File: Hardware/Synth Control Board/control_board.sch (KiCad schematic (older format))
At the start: 44 parts, among them J1 Conn_01x13, J2 Conn_01x03, J3 Conn_01x13, J4 Conn_01x13, J5 Conn_01x02, J6 Conn_01x13, SW1 SW_DPDT_x2, SW10 SW_SPST, SW11 SW_SPST, SW12 SW_SPST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

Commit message: add frequency and LFO connectors to control board
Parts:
- added J10, J7, J8, J9: Conn_01x05, Pin_Headers:Pin_Header_Straight_1x05_Pitch2.54mm, symbol Conn_01x05
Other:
- moved on the sheet: J2, J5, RV5, SW1A
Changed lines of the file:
@@
 L POT RV5
 U 1 1 5C5C948E
-P 1500 6350
-F 0 "RV5" V 1325 6350 50  0000 C CNN
-F 1 "10kA" V 1400 6350 50  0000 C CNN
-F 2 "Potentiometers:Potentiometer_Bourns_PTV09A-1_Horizontal" H 1500 6350 50  0001 C CNN
-F 3 "" H 1500 6350 50  0001 C CNN
-	1    1500 6350
+P 1500 5800
+F 0 "RV5" V 1325 5800 50  0000 C CNN
+F 1 "10kA" V 1400 5800 50  0000 C CNN
+F 2 "Potentiometers:Potentiometer_Bourns_PTV09A-1_Horizontal" H 1500 5800 50  0001 C CNN
+F 3 "" H 1500 5800 50  0001 C CNN
+	1    1500 5800
 	0    1    1    0
 $EndComp
@@
 Text Label 3000 7150 2    60   ~ 0
 freq_in_4
-Text Label 13000 2600 2    60   ~ 0
+Text Label 10400 3850 2    60   ~ 0
 freq_in_1
 Text Label 4250 5650 0    60   ~ 0
@@
 Text Label 4250 7150 0    60   ~ 0
 freq_out_4
-Text Label 13000 2800 2    60   ~ 0
+Text Label 10400 4050 2    60   ~ 0
 freq_out_1
-Text Label 1150 6350 2    60   ~ 0
+Text Label 1150 5800 2    60   ~ 0
 LFO_freq_in
-Text Label 1750 6350 0    60   ~ 0
+Text Label 1750 5800 0    60   ~ 0
 LFO_freq_out
-Text Label 10450 5200 2    60   ~ 0
+Text Label 1550 6400 2    60   ~ 0
 LFO_freq_in
-Text Label 10450 5300 2    60   ~ 0
+Text Label 1550 6500 2    60   ~ 0
 LFO_freq_out
 $Comp
@@
 L Conn_01x02 J5
 U 1 1 5C5CD696
-P 10800 5200
-F 0 "J5" H 10800 5300 50  0000 C CNN
-F 1 "Conn_01x02" H 10800 5000 50  0000 C CNN
-F 2 "Pin_Headers:Pin_Header_Straight_1x02_Pitch2.54mm" H 10800 5200 50  0001 C CNN
-F 3 "" H 10800 5200 50  0001 C CNN
-	1    10800 5200
-	1    0    0    -1
-$EndComp
-Wire Wire Line
-	10600 5200 10450 5200
-Wire Wire Line
-	10450 5300 10600 5300
+P 1900 6400
+F 0 "J5" H 1900 6500 50  0000 C CNN
+F 1 "Conn_01x02" H 1900 6200 50  0000 C CNN
+F 2 "Pin_Headers:Pin_Header_Straight_1x02_Pitch2.54mm" H 1900 6400 50  0001 C CNN
+F 3 "" H 1900 6400 50  0001 C CNN
+	1    1900 6400
+	1    0    0    -1
+$EndComp
+Wire Wire Line
+	1700 6400 1550 6400
+Wire Wire Line
+	1550 6500 1700 6500
 Wire Wire Line
 	3350 5450 3350 5400
@@
 Connection ~ 3650 7150
 Wire Wire Line
-	1500 6500 1500 6550
-Wire Wire Line
-	1500 6550 1300 6550
-Wire Wire Line
-	1300 6550 1300 6350
-Wire Wire Line
-	1150 6350 1350 6350
-Connection ~ 1300 6350
-Wire Wire Line
-	1750 6350 1650 6350
+	1500 5950 1500 6000
+Wire Wire Line
+	1500 6000 1300 6000
+Wire Wire Line
+	1300 6000 1300 5800
+Wire Wire Line
+	1150 5800 1350 5800
+Connection ~ 1300 5800
+Wire Wire Line
+	1750 5800 1650 5800
 $Comp
 L +5V #PWR024
@@
 	3550 6850 3550 7150
 Connection ~ 3550 7150
-Text Label 13000 2700 2    60   ~ 0
+Text Label 10400 3950 2    60   ~ 0
 freq_fb_1
 $Comp
 L SW_DPDT_x2 SW1
 U 1 1 5C5E11B0
-P 10050 5950
-F 0 "SW1" H 10050 6120 50  0000 C CNN
-F 1 "SW_DPDT_x2" H 10300 5950 50  0000 C CNN
-F 2 "SparkFun-Electromechanical:SWITCH-SPDT" H 10050 5950 50  0001 C CNN
-F 3 "" H 10050 5950 50  0001 C CNN
-	1    10050 5950
+P 1150 7150
+F 0 "SW1" H 1150 7320 50  0000 C CNN
+F 1 "SW_DPDT_x2" H 1400 7150 50  0000 C CNN
+F 2 "SparkFun-Electromechanical:SWITCH-SPDT" H 1150 7150 50  0001 C CNN
+F 3 "" H 1150 7150 50  0001 C CNN
+	1    1150 7150
 	-1   0    0    -1
 $EndComp
@@
 L Conn_01x03 J2
 U 1 1 5C5E130C
-P 10900 5950
-F 0 "J2" H 10900 6150 50  0000 C CNN
-F 1 "Conn_01x03" H 10900 5750 50  0000 C CNN
-F 2 "Pin_Headers:Pin_Header_Straight_1x03_Pitch2.54mm" H 10900 5950 50  0001 C CNN
-F 3 "" H 10900 5950 50  0001 C CNN
-	1    10900 5950
-	1    0    0    -1
-$EndComp
-Wire Wire Line
-	10700 5950 10250 5950
-Wire Wire Line
-	10700 5850 10400 5850
-Wire Wire Line
-	10400 5850 10400 5700
-Wire Wire Line
-	10400 5700 9750 5700
-Wire Wire Line
-	9750 5700 9750 5850
-Wire Wire Line
-	9750 5850 9850 5850
-Wire Wire Line
-	9850 6050 9750 6050
-Wire Wire Line
-	9750 6050 9750 6250
-Wire Wire Line
-	9750 6250 10400 6250
-Wire Wire Line
-	10400 6250 10400 6050
-Wire Wire Line
-	10400 6050 10700 6050
-Text Label 9850 5700 0    60   ~ 0
+P 2000 7150
+F 0 "J2" H 2000 7350 50  0000 C CNN
+F 1 "Conn_01x03" H 2000 6950 50  0000 C CNN
+F 2 "Pin_Headers:Pin_Header_Straight_1x03_Pitch2.54mm" H 2000 7150 50  0001 C CNN
+F 3 "" H 2000 7150 50  0001 C CNN
+	1    2000 7150
+	1    0    0    -1
+$EndComp
+Wire Wire Line
+	1800 7150 1350 7150
+Wire Wire Line
+	1800 7050 1500 7050
+Wire Wire Line
+	1500 7050 1500 6900
+Wire Wire Line
+	1500 6900 850  6900
+Wire Wire Line
+	850  6900 850  7050
+Wire Wire Line
+	850  7050 950  7050
+Wire Wire Line
+	950  7250 850  7250
+Wire Wire Line
+	850  7250 850  7450
+Wire Wire Line
+	850  7450 1500 7450
+Wire Wire Line
+	1500 7450 1500 7250
+Wire Wire Line
+	1500 7250 1800 7250
+Text Label 950  6900 0    60   ~ 0
 LFO_square
-Text Label 9950 6250 0    60   ~ 0
+Text Label 1050 7450 0    60   ~ 0
 LFO_tri
-Text Label 10300 5950 0    60   ~ 0
+Text Label 1400 7150 0    60   ~ 0
 LFO_out
 $Comp
@@
 Wire Wire Line
 	6700 5750 6950 5750
-Text Label 13000 2900 2    60   ~ 0
+Text Label 10400 4150 2    60   ~ 0
 lfo_in_1
-Text Label 13000 3000 2    60   ~ 0
+Text Label 10400 4250 2    60   ~ 0
 lfo_out_1
 $Comp
@@
 Text Label 7250 2750 2    60   ~ 0
 osc2_quant
-Text Label 12600 3600 0    60   ~ 0
+Text Label 10400 4500 2    60   ~ 0
 freq_in_2
-Text Label 12600 3400 0    60   ~ 0
+Text Label 10400 4700 2    60   ~ 0
 freq_out_2
 $Comp
@@
 	0    1    -1   0
 $EndComp
-Text Label 12600 3500 0    60   ~ 0
+Text Label 10400 4600 2    60   ~ 0
 freq_fb_2
-Text Label 12600 3700 0    60   ~ 0
+Text Label 10400 4800 2    60   ~ 0
 lfo_in_2
-Text Label 12600 3800 0    60   ~ 0
+Text Label 10400 4900 2    60   ~ 0
 lfo_out_2
 $Comp
@@
 Text Label 8800 2400 2    60   ~ 0
 osc3_quant
-Text Label 14100 3150 2    60   ~ 0
+Text Label 10400 5200 2    60   ~ 0
 freq_in_3
-Text Label 14100 2950 2    60   ~ 0
+Text Label 10400 5400 2    60   ~ 0
 freq_out_3
 $Comp
@@
 	0    1    -1   0
 $EndComp
-Text Label 14100 3050 2    60   ~ 0
+Text Label 10400 5300 2    60   ~ 0
 freq_fb_3
-Text Label 14100 3350 2    60   ~ 0
+Text Label 10400 5500 2    60   ~ 0
 lfo_in_3
-Text Label 14100 3250 2    60   ~ 0
+Text Label 10400 5600 2    60   ~ 0
 lfo_out_3
 $Comp
@@
 Text Label 10400 2400 2    60   ~ 0
 osc4_quant
-Text Label 14600 3150 0    60   ~ 0
+Text Label 10400 5900 2    60   ~ 0
 freq_in_4
-Text Label 14600 2950 0    60   ~ 0
+Text Label 10400 6100 2    60   ~ 0
 freq_out_4
 $Comp
@@
 	0    1    -1   0
 $EndComp
-Text Label 14600 3050 0    60   ~ 0
+Text Label 10400 6000 2    60   ~ 0
 freq_fb_4
-Text Label 14600 3250 0    60   ~ 0
+Text Label 10400 6200 2    60   ~ 0
 lfo_in_4
-Text Label 14600 3350 0    60   ~ 0
+Text Label 10400 6300 2    60   ~ 0
 lfo_out_4
 $Comp
@@
 	1    0    0    -1
 $EndComp
+$Comp
+L Conn_01x05 J7
+U 1 1 5C63B7E7
+P 10600 4050
+F 0 "J7" H 10600 4350 50  0000 C CNN
+F 1 "Conn_01x05" H 10600 3750 50  0000 C CNN
+F 2 "Pin_Headers:Pin_Header_Straight_1x05_Pitch2.54mm" H 10600 4050 50  0001 C CNN
+F 3 "" H 10600 4050 50  0001 C CNN
+	1    10600 4050
+	1    0    0    -1
+$EndComp
+$Comp
+L Conn_01x05 J8
+U 1 1 5C63B889
+P 10600 4700
+F 0 "J8" H 10600 5000 50  0000 C CNN
+F 1 "Conn_01x05" H 10600 4400 50  0000 C CNN
+F 2 "Pin_Headers:Pin_Header_Straight_1x05_Pitch2.54mm" H 10600 4700 50  0001 C CNN
+F 3 "" H 10600 4700 50  0001 C CNN
+	1    10600 4700
+	1    0    0    -1
+$EndComp
+$Comp
+L Conn_01x05 J9
+U 1 1 5C63BBB5
+P 10600 5400
+F 0 "J9" H 10600 5700 50  0000 C CNN
+F 1 "Conn_01x05" H 10600 5100 50  0000 C CNN
+F 2 "Pin_Headers:Pin_Header_Straight_1x05_Pitch2.54mm" H 10600 5400 50  0001 C CNN
+F 3 "" H 10600 5400 50  0001 C CNN
+	1    10600 5400
+	1    0    0    -1
+$EndComp
+$Comp
+L Conn_01x05 J10
+U 1 1 5C63BC62
+P 10600 6100
+F 0 "J10" H 10600 6400 50  0000 C CNN
+F 1 "Conn_01x05" H 10600 5800 50  0000 C CNN
+F 2 "Pin_Headers:Pin_Header_Straight_1x05_Pitch2.54mm" H 10600 6100 50  0001 C CNN
+F 3 "" H 10600 6100 50  0001 C CNN
+	1    10600 6100
+	1    0    0    -1
+$EndComp

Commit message: match relative connector placement between two boards
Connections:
- net labels removed: GNDD

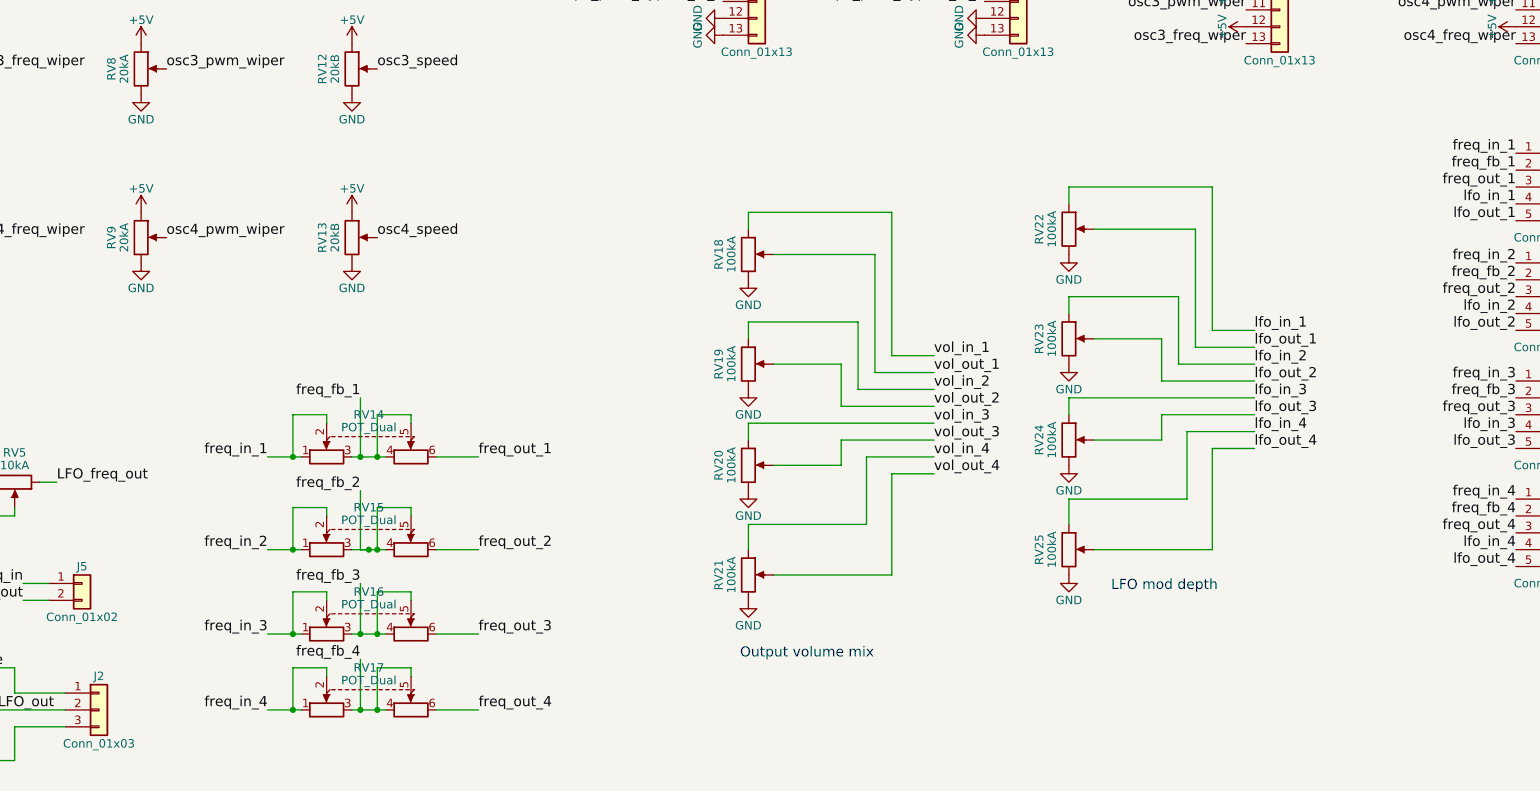
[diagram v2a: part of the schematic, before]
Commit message: add delay connector to main board and route it.
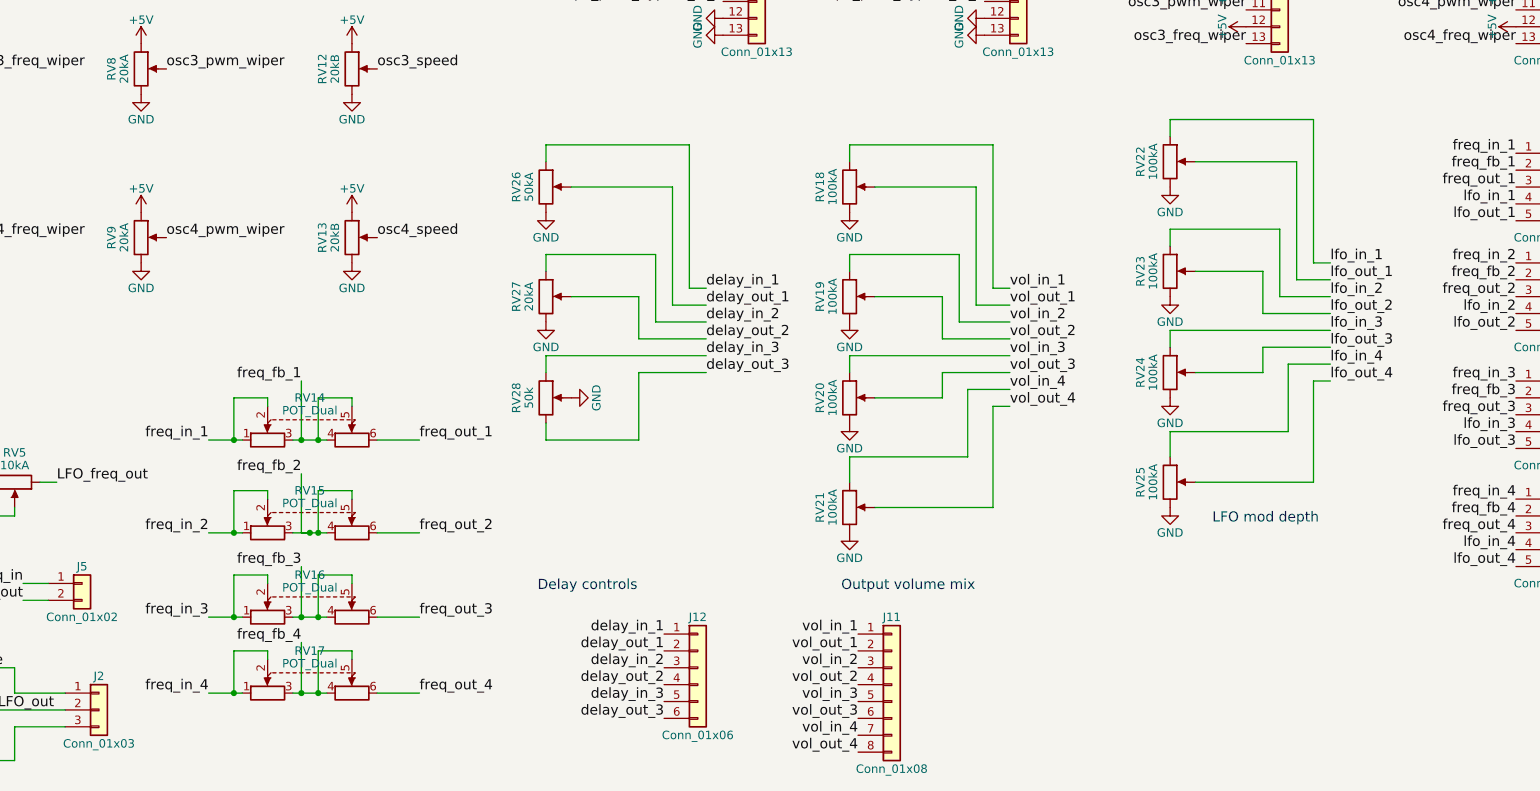
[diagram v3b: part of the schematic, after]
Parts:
- added J11: Conn_01x08, Pin_Headers:Pin_Header_Straight_1x08_Pitch2.54mm, symbol Conn_01x08
- added J12: Conn_01x06, Pin_Headers:Pin_Header_Straight_1x06_Pitch2.54mm, symbol Conn_01x06
- added RV26: 50kA, Potentiometers:Potentiometer_Bourns_PTV09A-1_Horizontal, symbol POT
- added RV27: 20kA, Potentiometers:Potentiometer_Bourns_PTV09A-1_Horizontal, symbol POT
- added RV28: 50k, Potentiometers:Potentiometer_Bourns_PTV09A-1_Horizontal, symbol POT
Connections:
- net GND: now also RV26.3, RV27.3, RV28.2
- net vol_in_1: now also J11.1 (Pin_1)
- net vol_in_2: now also J11.3 (Pin_3)
- net vol_in_3: now also J11.5 (Pin_5)
- net vol_in_4: now also J11.7 (Pin_7)
- net vol_out_1: now also J11.2 (Pin_2)
- net vol_out_2: now also J11.4 (Pin_4)
- net vol_out_3: now also J11.6 (Pin_6)
- net vol_out_4: now also J11.8 (Pin_8)
- new net delay_in_1: J12.1 (Pin_1), RV26.1
- new net delay_in_2: J12.3 (Pin_3), RV27.1
- new net delay_in_3: J12.5 (Pin_5), RV28.1
- new net delay_out_1: J12.2 (Pin_2), RV26.2
- new net delay_out_2: J12.4 (Pin_4), RV27.2
- new net delay_out_3: J12.6 (Pin_6), RV28.3
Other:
- note added: "Delay controls"
- moved on the sheet: RV14, RV15, RV16, RV17, RV18, RV19, RV20, RV21, RV22, RV23, RV24, RV25

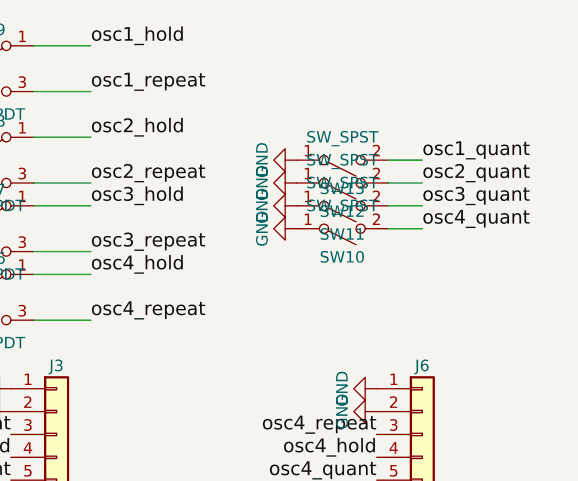
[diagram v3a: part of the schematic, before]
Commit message: fix delay controls on panel artwork and control board layout
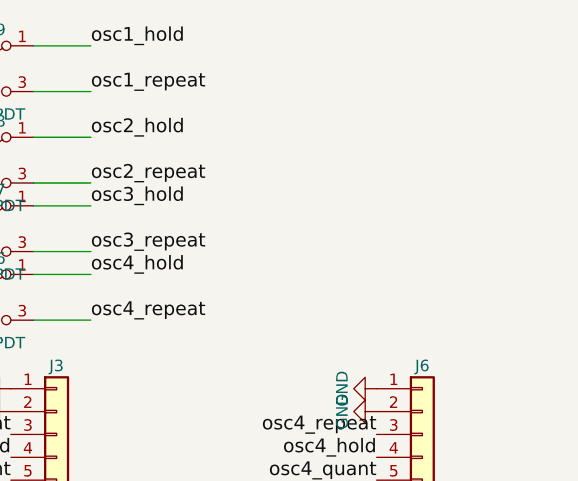
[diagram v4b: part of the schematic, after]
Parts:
- removed SW10, SW11, SW12, SW13: SW_SPST, SparkFun-Electromechanical:SWITCH-SPDT, symbol SW_SPST
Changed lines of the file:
@@
 Text Label 9150 1700 0    60   ~ 0
 osc4_repeat
-$Comp
-L SW_SPST SW13
-U 1 1 5C54E122
-P 10250 1000
-F 0 "SW13" H 10250 1125 50  0000 C CNN
-F 1 "SW_SPST" H 10250 900 50  0000 C CNN
-F 2 "SparkFun-Electromechanical:SWITCH-SPDT" H 10250 1000 50  0001 C CNN
-F 3 "" H 10250 1000 50  0001 C CNN
-	1    10250 1000
-	1    0    0    1
-$EndComp
-$Comp
-L SW_SPST SW12
-U 1 1 5C54E07F
-P 10250 1100
-F 0 "SW12" H 10250 1225 50  0000 C CNN
-F 1 "SW_SPST" H 10250 1000 50  0000 C CNN
-F 2 "SparkFun-Electromechanical:SWITCH-SPDT" H 10250 1100 50  0001 C CNN
-F 3 "" H 10250 1100 50  0001 C CNN
-	1    10250 1100
-	1    0    0    1
-$EndComp
-$Comp
-L SW_SPST SW11
-U 1 1 5C54DFDF
-P 10250 1200
-F 0 "SW11" H 10250 1325 50  0000 C CNN
-F 1 "SW_SPST" H 10250 1100 50  0000 C CNN
-F 2 "SparkFun-Electromechanical:SWITCH-SPDT" H 10250 1200 50  0001 C CNN
-F 3 "" H 10250 1200 50  0001 C CNN
-	1    10250 1200
-	1    0    0    1
-$EndComp
-$Comp
-L SW_SPST SW10
-U 1 1 5C54DEFF
-P 10250 1300
-F 0 "SW10" H 10250 1425 50  0000 C CNN
-F 1 "SW_SPST" H 10250 1200 50  0000 C CNN
-F 2 "SparkFun-Electromechanical:SWITCH-SPDT" H 10250 1300 50  0001 C CNN
-F 3 "" H 10250 1300 50  0001 C CNN
-	1    10250 1300
-	1    0    0    1
-$EndComp
-Text Label 10600 1000 0    60   ~ 0
-osc1_quant
-Text Label 10600 1100 0    60   ~ 0
-osc2_quant
-Text Label 10600 1200 0    60   ~ 0
-osc3_quant
-Text Label 10600 1300 0    60   ~ 0
-osc4_quant
 Text Label 6000 1300 2    60   ~ 0
 envelope_pwm_bypass_in_4
@@
 Text Label 5700 2750 2    60   ~ 0
 osc1_quant
-Wire Wire Line
-	10600 1300 10450 1300
-Wire Wire Line
-	10450 1200 10600 1200
-Wire Wire Line
-	10600 1100 10450 1100
-Wire Wire Line
-	10450 1000 10600 1000
 Text Label 2650 5550 2    60   ~ 0
 freq_in_1
@@
 	0    1    1    0
 $EndComp
-$Comp
-L GND #PWR057
-U 1 1 5C638574
-P 10050 1000
-F 0 "#PWR057" H 10050 750 50  0001 C CNN
-F 1 "GND" H 10050 850 50  0000 C CNN
-F 2 "" H 10050 1000 50  0001 C CNN
-F 3 "" H 10050 1000 50  0001 C CNN
-	1    10050 1000
-	0    1    1    0
-$EndComp
-$Comp
-L GND #PWR058
-U 1 1 5C63860F
-P 10050 1100
-F 0 "#PWR058" H 10050 850 50  0001 C CNN
-F 1 "GND" H 10050 950 50  0000 C CNN
-F 2 "" H 10050 1100 50  0001 C CNN
-F 3 "" H 10050 1100 50  0001 C CNN
-	1    10050 1100
-	0    1    1    0
-$EndComp
-$Comp
-L GND #PWR059
-U 1 1 5C6386AA
-P 10050 1200
-F 0 "#PWR059" H 10050 950 50  0001 C CNN
-F 1 "GND" H 10050 1050 50  0000 C CNN
-F 2 "" H 10050 1200 50  0001 C CNN
-F 3 "" H 10050 1200 50  0001 C CNN
-	1    10050 1200
-	0    1    1    0
-$EndComp
-$Comp
-L GND #PWR060
-U 1 1 5C638745
-P 10050 1300
-F 0 "#PWR060" H 10050 1050 50  0001 C CNN
-F 1 "GND" H 10050 1150 50  0000 C CNN
-F 2 "" H 10050 1300 50  0001 C CNN
-F 3 "" H 10050 1300 50  0001 C CNN
-	1    10050 1300
-	0    1    1    0
-$EndComp

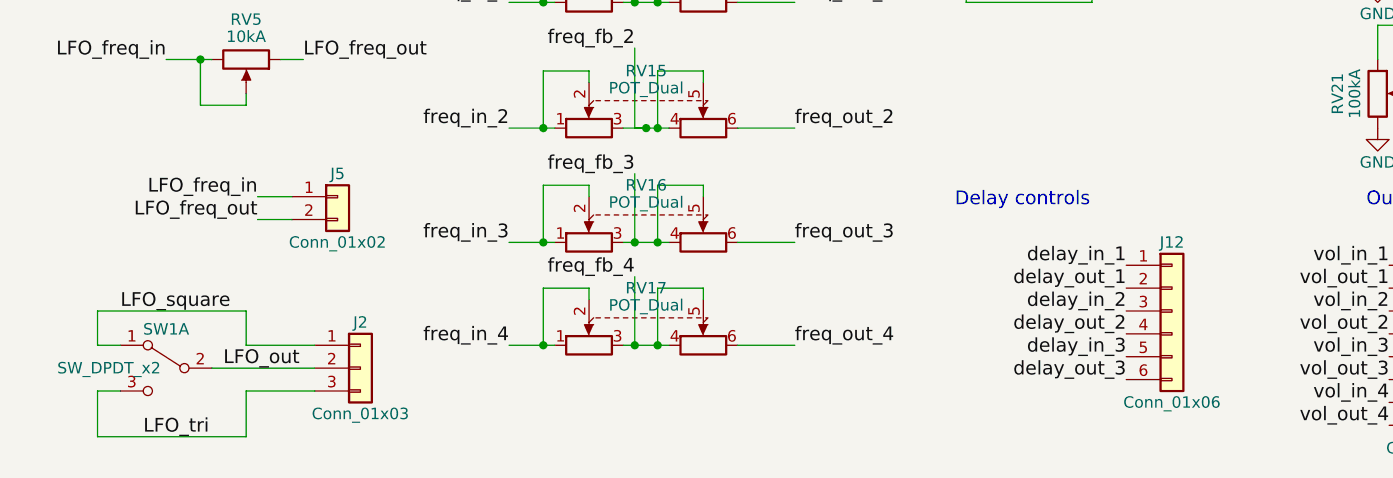
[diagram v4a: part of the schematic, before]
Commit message: move main synth board so that connector dimensions match between boards.
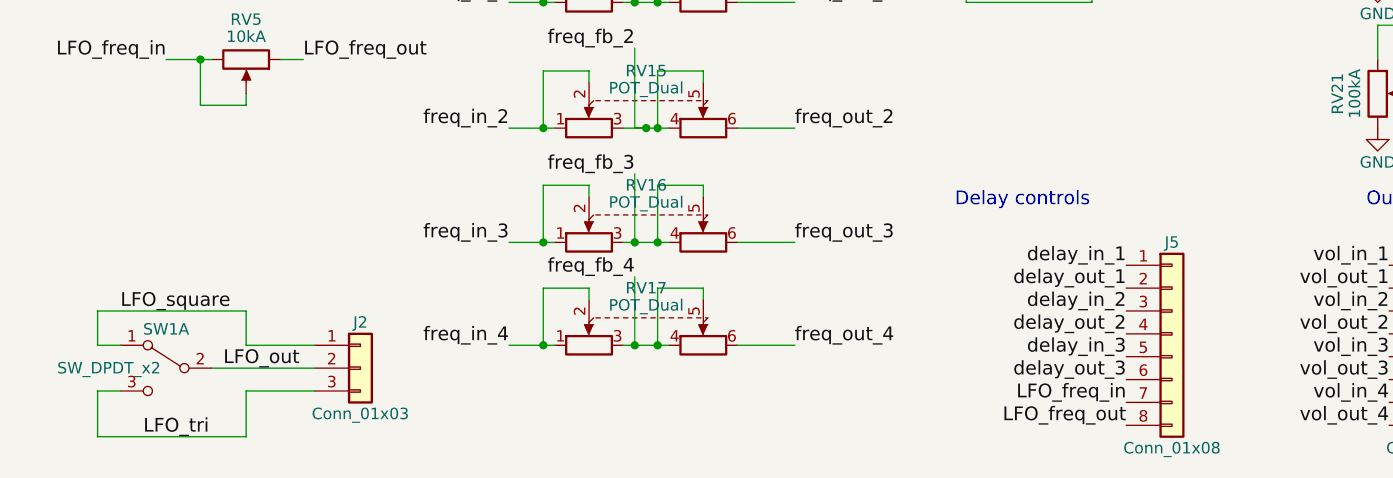
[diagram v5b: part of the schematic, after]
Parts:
- removed J12: Conn_01x06, Pin_Headers:Pin_Header_Straight_1x06_Pitch2.54mm, symbol Conn_01x06
- removed J5: Conn_01x02, Pin_Headers:Pin_Header_Straight_1x02_Pitch2.54mm, symbol Conn_01x02
- added J5: Conn_01x08, Pin_Headers:Pin_Header_Straight_1x08_Pitch2.54mm, symbol Conn_01x08
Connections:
- net LFO_freq_in: now also J5.7 (Pin_7)
- net LFO_freq_out: now also J5.8 (Pin_8)
- net delay_in_1: now also J5.1 (Pin_1)
- net delay_in_2: now also J5.3 (Pin_3)
- net delay_in_3: now also J5.5 (Pin_5)
- net delay_out_1: now also J5.2 (Pin_2)
- net delay_out_2: now also J5.4 (Pin_4)
- net delay_out_3: now also J5.6 (Pin_6)
